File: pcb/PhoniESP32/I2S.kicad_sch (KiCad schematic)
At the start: 7 parts, among them J5 Screw_Terminal_01x02, U2 MAX98357AETE+T, U4 SPH0645LM4H-1-8_C19272537

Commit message: fix(pcb): add power flags for ERC
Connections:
- no-connect marks 4 -> 5
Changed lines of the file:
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@@
+	)
+	(no_connect
+		(at 74.93 45.72)
 	)
 	(no_connect

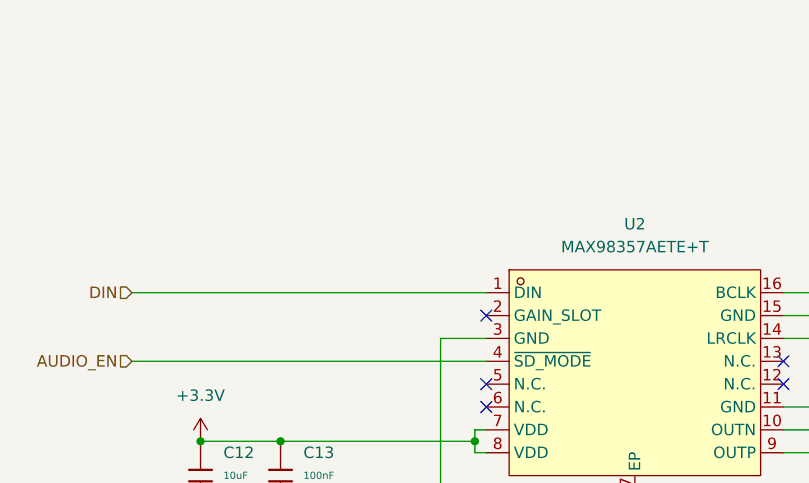
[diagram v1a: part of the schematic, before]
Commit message: feat(pcb): place test points and placeholders
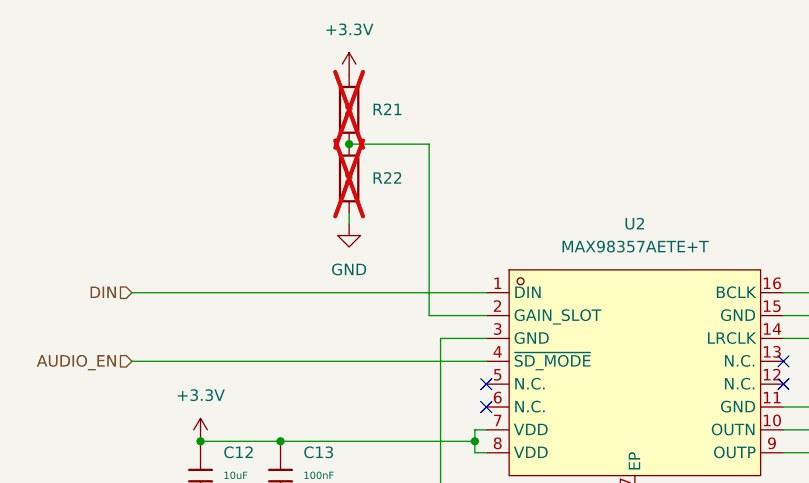
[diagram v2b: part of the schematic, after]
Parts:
- added R21, R22: 0Ω, PCM_JLCPCB:R_0603, symbol PCM_JLCPCB-Resistors:0603,0Ω
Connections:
- net +3.3V: now also R21.1
- net GND: now also R22.2
- net at U2.2 (GAIN_SLOT): now also R21.2, R22.1
- no-connect marks 5 -> 4

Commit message: chore(pcb): final cleanups
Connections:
- net SPK-: now reaches J5.1 (Pin_1), U2.10 (OUTN)
- net SPK+: now reaches J5.2 (Pin_2), U2.9 (OUTP)
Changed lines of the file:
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@@
+		)
+	)
+	(label "SPK+"
+		(at 109.22 60.96 0)
+		(effects
+			(font
+				(size 1.27 1.27)
+			)
+			(justify left bottom)
+		)
+	)
+	(label "SPK-"
+		(at 109.22 58.42 0)
+		(effects
+			(font
+				(size 1.27 1.27)
+			)
+			(justify left bottom)
 		)
 	)

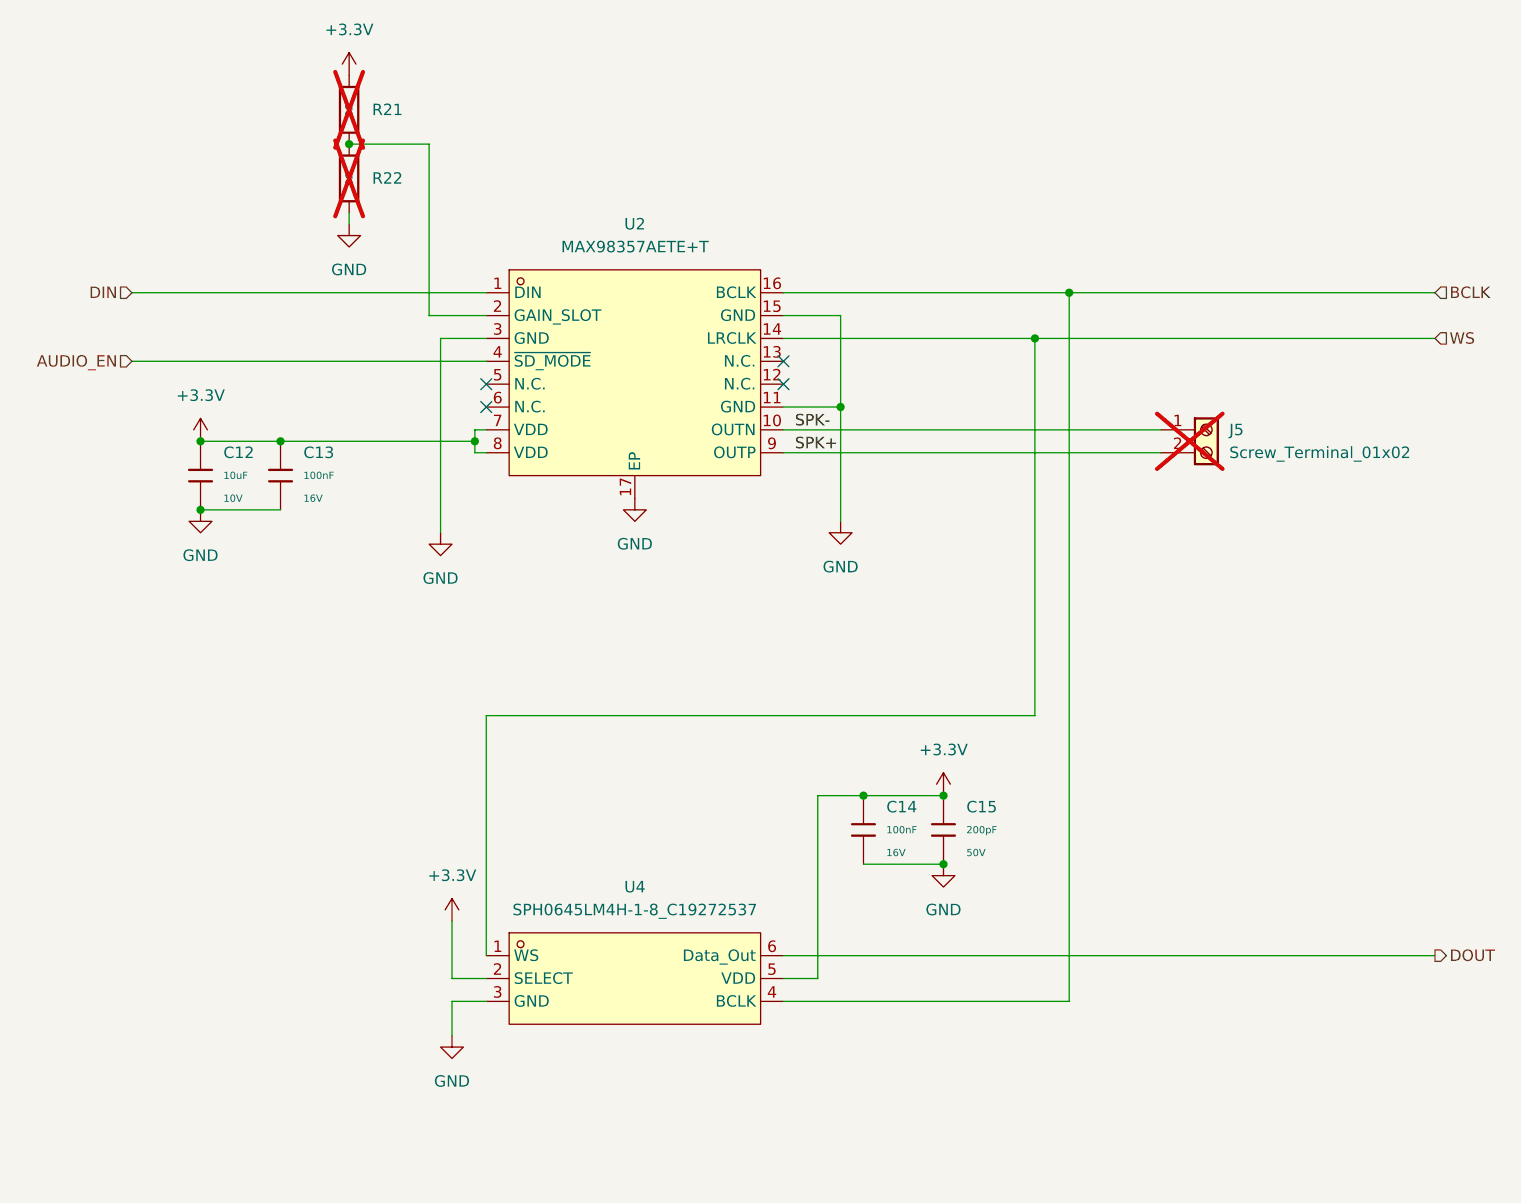
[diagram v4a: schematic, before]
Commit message: fix(pcb): minor revisions by external reviewer
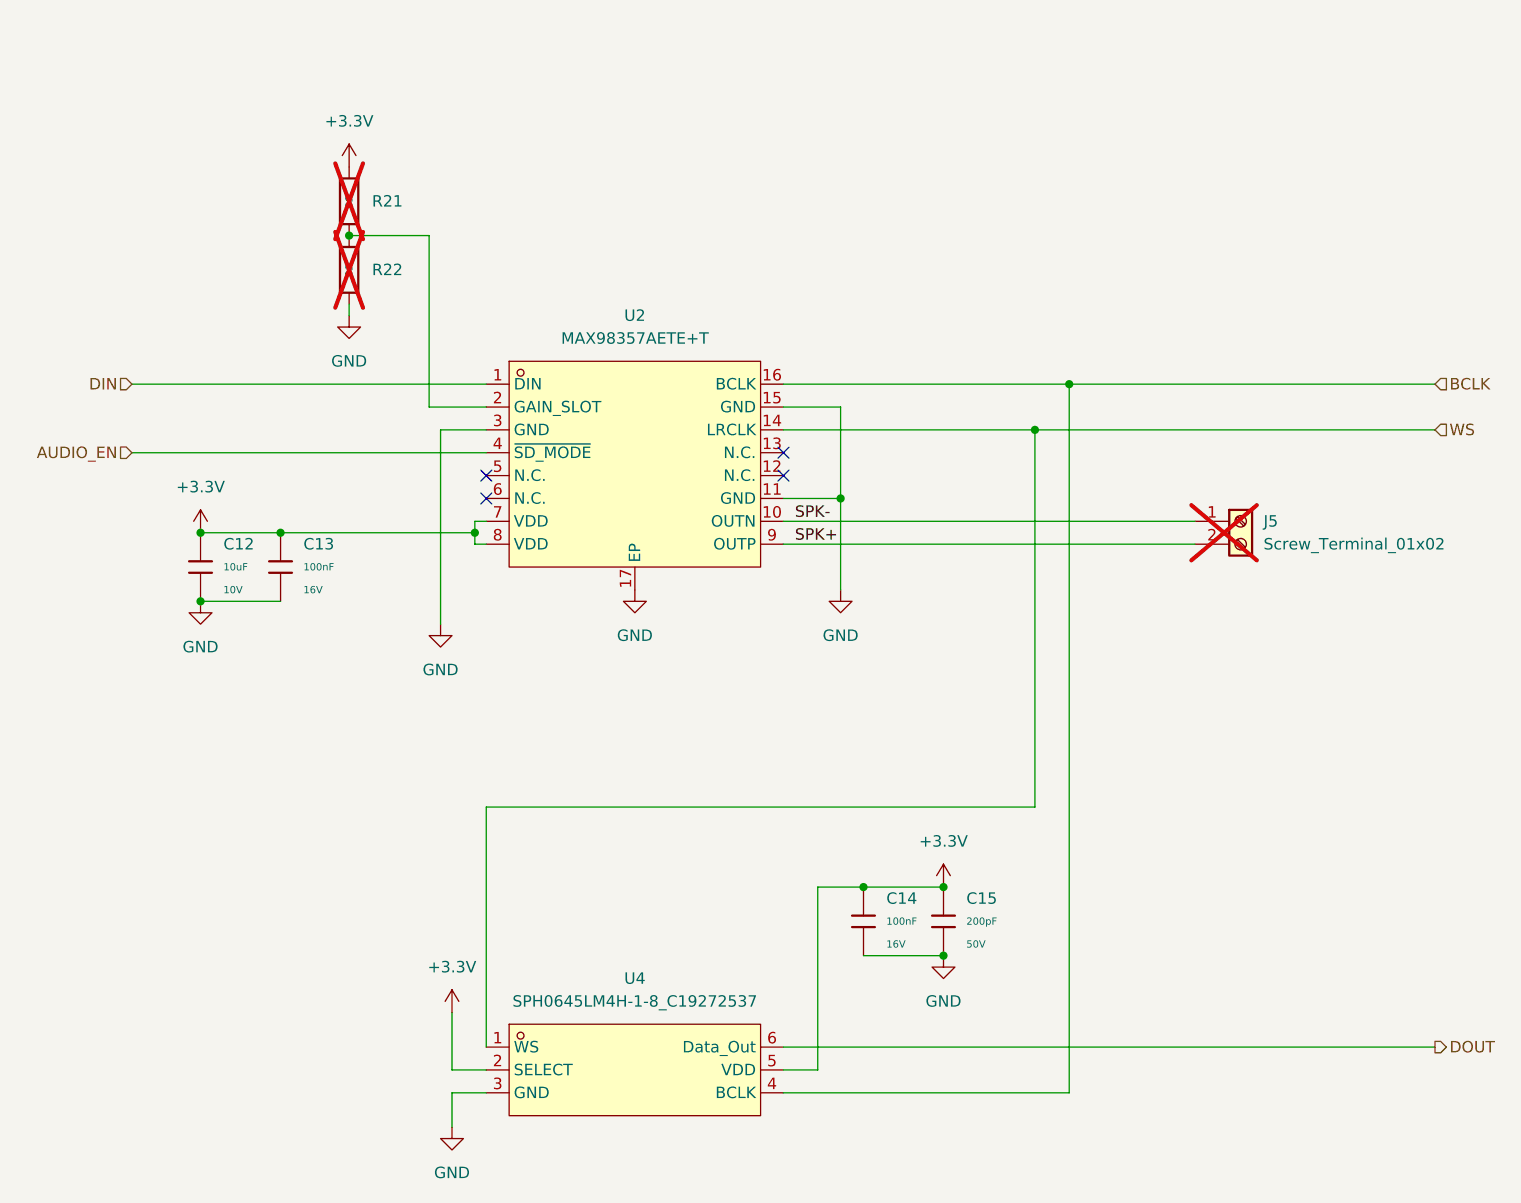
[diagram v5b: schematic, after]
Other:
- moved on the sheet: C12, C13, C14, C15, J5, R21, R22, U2, U4

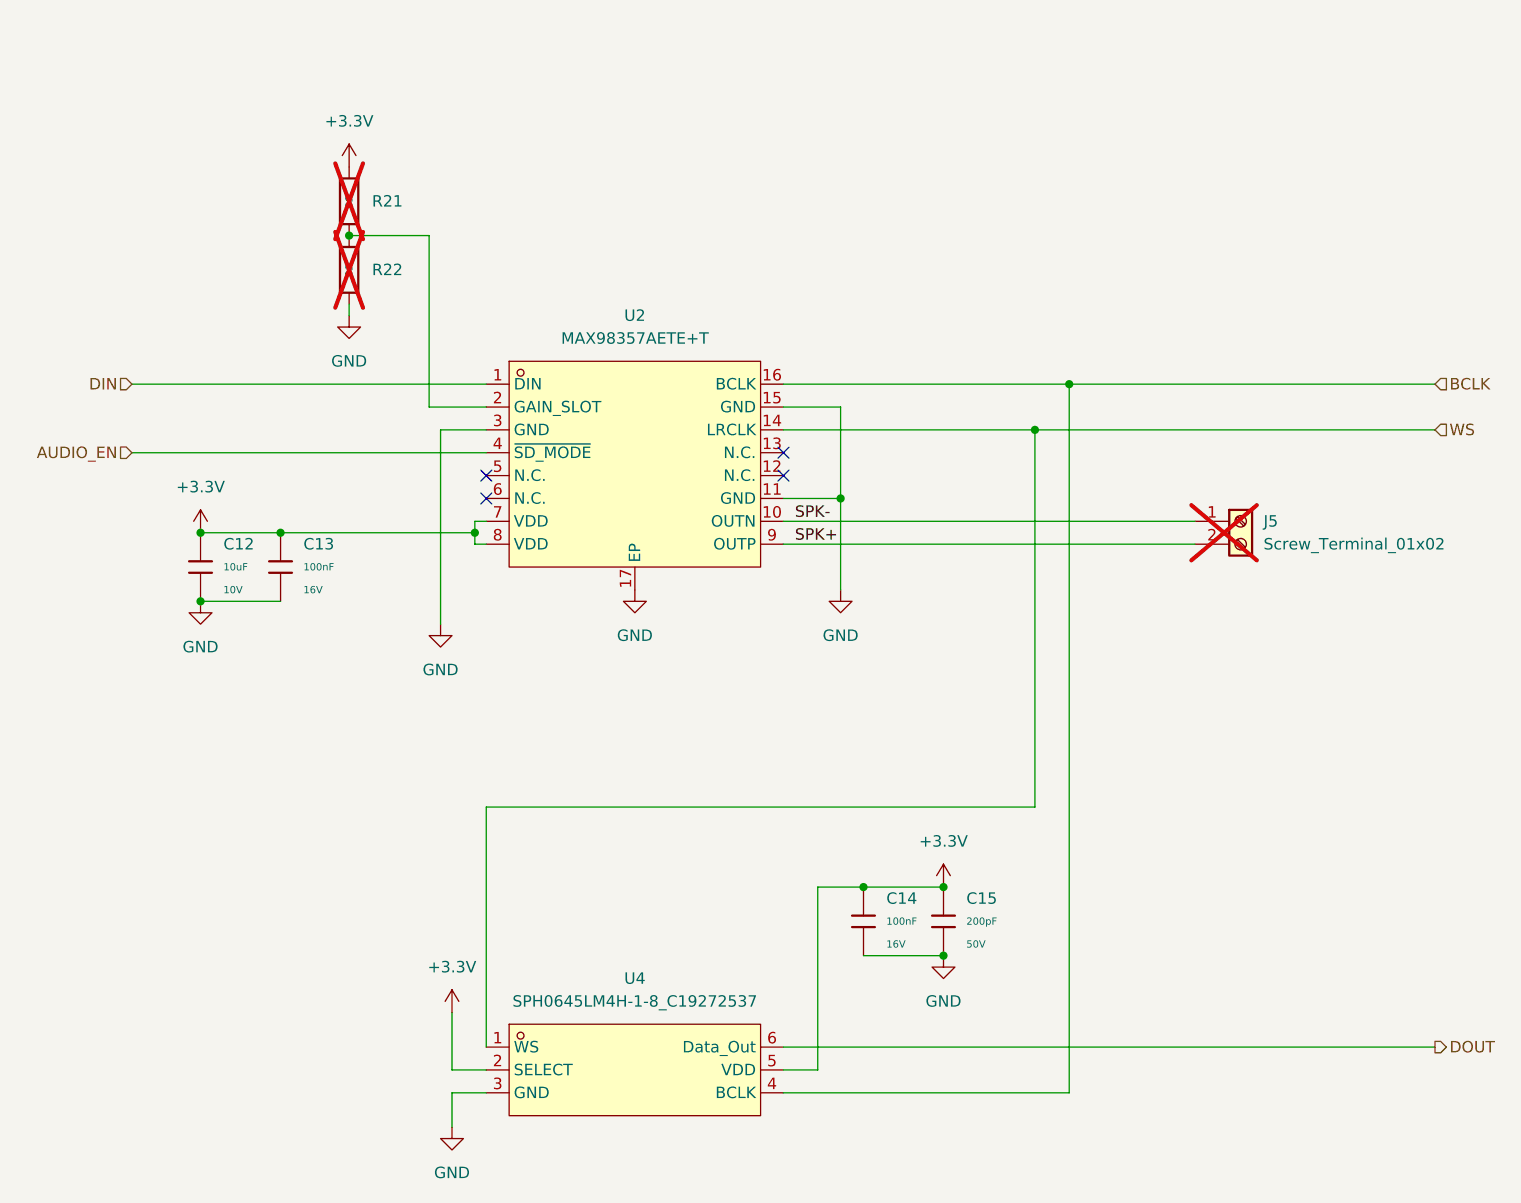
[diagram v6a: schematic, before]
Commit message: feat(pcb): version for hand soldering
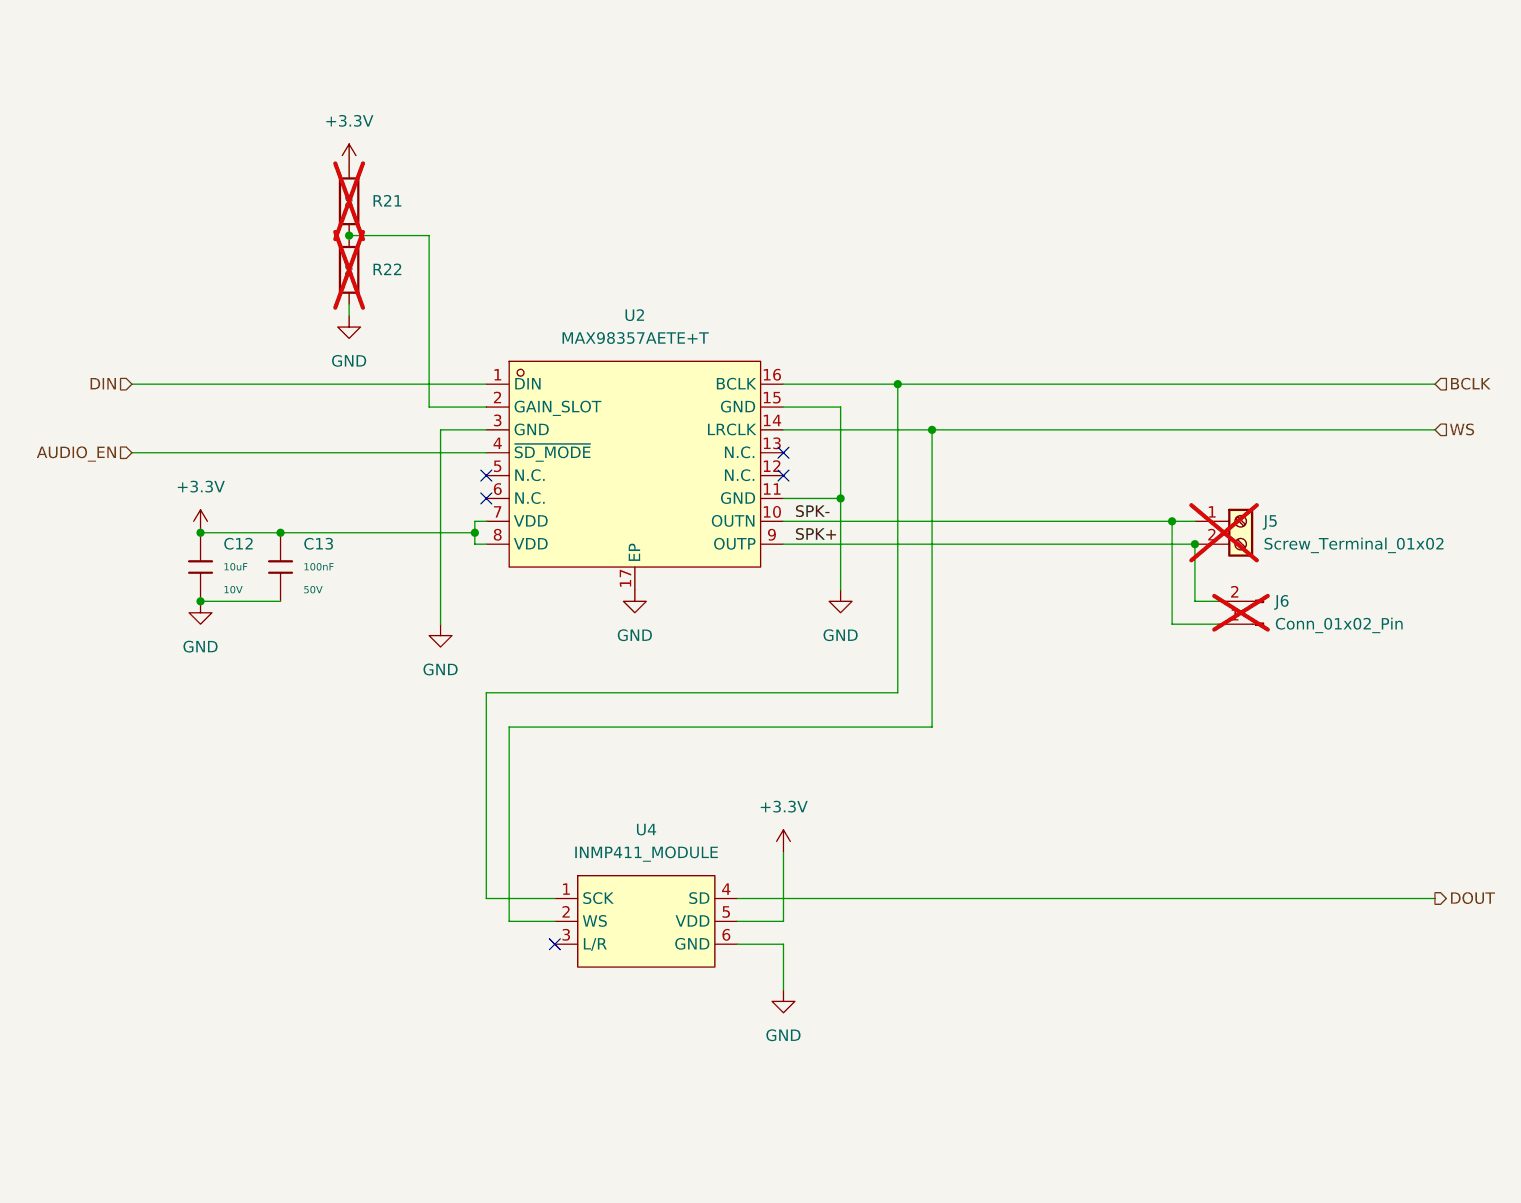
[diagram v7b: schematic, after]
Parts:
- removed C14: 100nF, PCM_JLCPCB:C_0402, symbol PCM_JLCPCB-Capacitors:0402,100nF
- removed C15: 200pF, PCM_JLCPCB:C_0603, symbol PCM_JLCPCB-Capacitors:0603,200pF
- removed U4: SPH0645LM4H-1-8_C19272537, JLCPCB:MIC-SMD_6P-L3.5-W2.7-P0.90-BL, symbol JLCPCB:SPH0645LM4H-1-8_C19272537
- added J6: Conn_01x02_Pin, Connector_JST:JST_PH_B2B-PH-K_1x02_P2.00mm_Vertical, symbol Connector:Conn_01x02_Pin
- added U4: INMP411_MODULE, JLCPCB:INMP411_MODULE, symbol JLCPCB:INMP441_MODULE
- C13: footprint PCM_JLCPCB:C_0402 -> PCM_JLCPCB:C_0603; symbol PCM_JLCPCB-Capacitors:0402,100nF -> PCM_JLCPCB-Capacitors:0603,100nF; LCSC C1525 -> C14663; Manufacturer Samsung Electro-Mechanics -> YAGEO; Part CL05B104KO5NNNC -> CC0603KRX7R9BB104; Price 0.004USD -> 0.006USD; Stock 20208285 -> 70324515; Voltage Rated 16V -> 50V
- J5: footprint TerminalBlock_4Ucon:TerminalBlock_4Ucon_1x02_P3.50mm_Horizontal -> TerminalBlock:TerminalBlock_Xinya_XY308-2.54-2P_1x02_P2.54mm_Horizontal
- U2: MPN (none) -> MAX98357AETE+T
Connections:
- net +3.3V: now also U4.5 (VDD)
- net BCLK: now also U4.1 (SCK)
- net DOUT: now also U4.4 (SD)
- net GND: now also U4.6 (GND)
- net SPK+: now also J6.2 (Pin_2)
- net SPK-: now also J6.1 (Pin_1)
- net WS: now also U4.2 (WS)
- no-connect marks 4 -> 5
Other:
- title: (none) -> PhoniESP32
